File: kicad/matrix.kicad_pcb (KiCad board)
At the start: 2 copper layers, 76.2 x 76.2 mm, 20 parts, among them J1 Conn_01x08, U1 TLC59025, U10 P-FET, U11 P-FET, U2 74HC595, U3 74HC595, U4 P-FET, U5 P-FET, U6 P-FET, U7 P-FET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

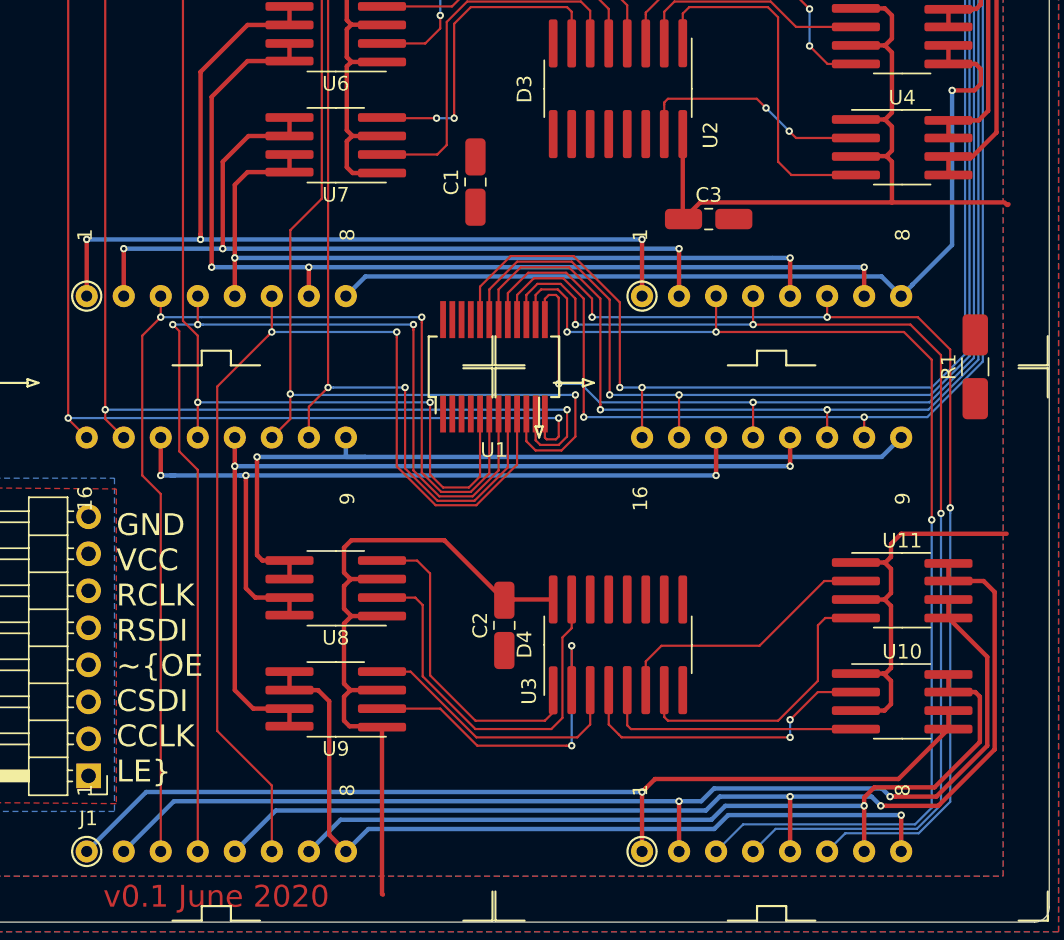
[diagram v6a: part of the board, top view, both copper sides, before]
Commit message: Wire up everything but ground net
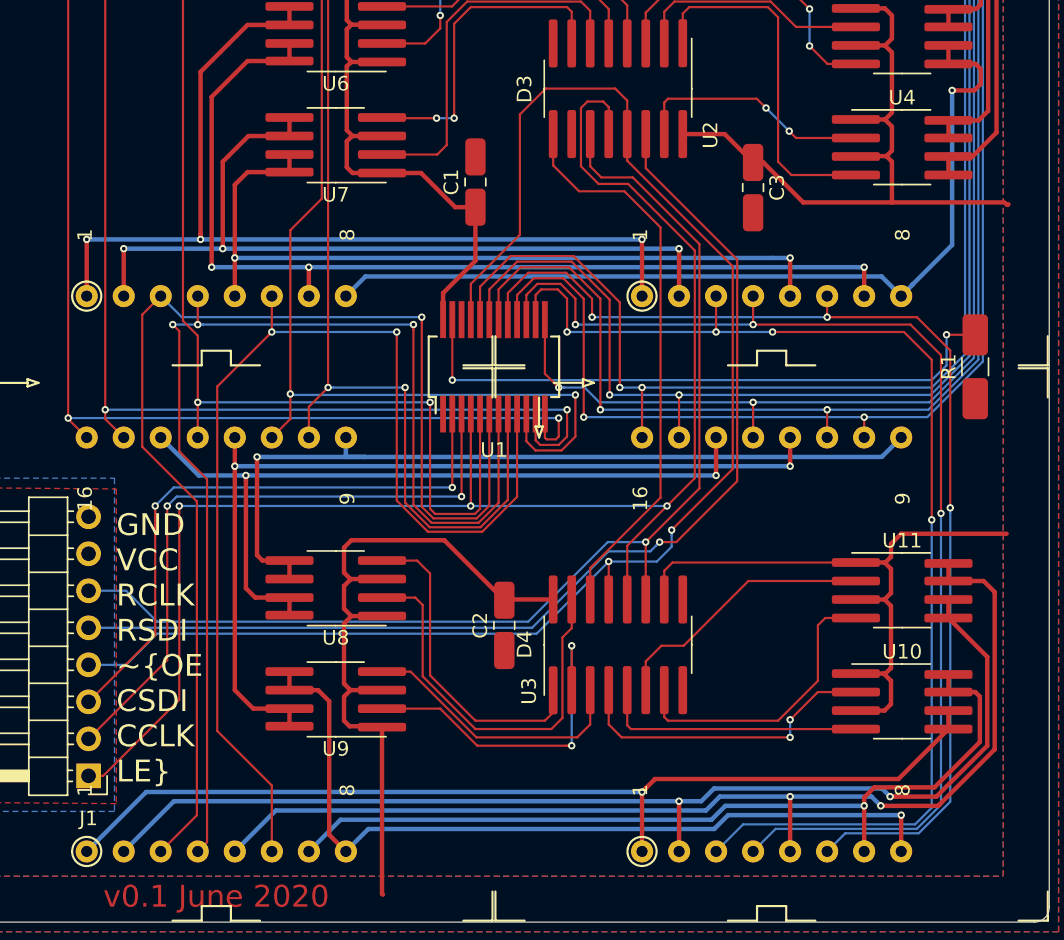
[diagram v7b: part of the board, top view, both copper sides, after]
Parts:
- moved C3 3.74 mm to (208.2, 63.1), turned to 270 degrees
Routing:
- net /~OE: track 0.00 -> 106.7 mm, vias 0 -> 2
- net /LE: track 0.00 -> 105.6 mm, vias 0 -> 3
- net /ROWCLK: track 0.00 -> 79.2 mm, vias 0 -> 1
- net /ROWSDI: track 0.00 -> 75.1 mm, vias 0 -> 1
- net /COLCLK: track 0.00 -> 44.3 mm, vias 0 -> 2
- net Net-(R1-Pad2): track 0.00 -> 42.5 mm, vias 0 -> 2
- net /COLSDI: track 0.00 -> 41.3 mm, vias 0 -> 2
- net Net-(U2-Pad9): track 0.00 -> 38.8 mm
- net VDD: track 161.7 -> 190.8 mm
- net /COL1: track 77.5 -> 84.3 mm, vias 2 -> 1
- net /COL2: track 76.5 -> 81.2 mm
- net /COL4: track 73.0 -> 77.2 mm
- net /COL3: track 62.6 -> 66.8 mm
- net /COL0: track 68.2 -> 72.4 mm
- net /COL8: track 85.6 -> 82.1 mm
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
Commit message: Wire up remaining traces
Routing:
- net GND: track 0.00 -> 166.3 mm, vias 0 -> 7
- net VDD: track 190.8 -> 205.3 mm, vias 0 -> 2
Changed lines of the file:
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@@
   (general
     (thickness 1.6)
-    (drawings 12)
-    (tracks 816)
+    (drawings 13)
+    (tracks 859)
     (zones 0)
     (modules 20)
@@
   (page A4)
   (layers
-    (0 F.Cu signal)
-    (31 B.Cu signal)
-    (36 B.SilkS user hide)
-    (37 F.SilkS user hide)
+    (0 F.Cu signal hide)
+    (31 B.Cu signal hide)
+    (36 B.SilkS user)
+    (37 F.SilkS user)
     (38 B.Mask user)
     (39 F.Mask user)
@@
     (user_trace_width 0.1524)
     (user_trace_width 0.3048)
+    (user_trace_width 0.762)
     (trace_clearance 0.1524)
     (zone_clearance 0.508)
@@
     (descr "Through hole angled pin header, 1x08, 2.54mm pitch, 6mm pin length, single row")
     (tags "Through hole angled pin header THT 1x08 2.54mm single row")
-    (fp_text reference J1 (at 0 -2.921) (layer F.SilkS)
+    (fp_text reference J1 (at 0 20.1676) (layer F.SilkS)
       (effects (font (size 1 1) (thickness 0.15)))
     )
@@
   (module local:LED_8x8_3MM_38x38MM (layer F.Cu)
     (at 209.423 56.388 90)
-    (fp_text reference D3 (at 0 -16.95 90) (layer F.SilkS)
+    (fp_text reference D3 (at 14.3256 11.557 180) (layer F.SilkS)
       (effects (font (size 1 1) (thickness 0.15)))
     )
@@
   (module local:LED_8x8_3MM_38x38MM (layer F.Cu)
     (at 171.323 56.388 90)
-    (fp_text reference D1 (at 0 -16.95 90) (layer F.SilkS)
+    (fp_text reference D1 (at 14.1986 11.43 180) (layer F.SilkS)
       (effects (font (size 1 1) (thickness 0.15)))
     )
@@
   (module local:LED_8x8_3MM_38x38MM (layer F.Cu)
     (at 171.323 94.491 90)
-    (fp_text reference D2 (at 0 -16.95 90) (layer F.SilkS)
+    (fp_text reference D2 (at -14.2464 11.43 180) (layer F.SilkS)
       (effects (font (size 1 1) (thickness 0.15)))
     )
@@
   (module local:LED_8x8_3MM_38x38MM (layer F.Cu)
     (at 209.423 94.488 90)
-    (fp_text reference D4 (at 0 -16.95 90) (layer F.SilkS)
+    (fp_text reference D4 (at -14.2494 11.43 180) (layer F.SilkS)
       (effects (font (size 1 1) (thickness 0.15)))
     )
@@
     )
   )
+  (gr_text "v0.1 June 2020" (at 154.305 94.6404 270) (layer B.Cu)
+    (effects (font (size 1.5 1.5) (thickness 0.3)) (justify mirror))
+  )
   (gr_text "GND\nVCC\nRCLK\nRSDI\n~OE\nCSDI\nCCLK\nLE" (at 160.401 94.742) (layer B.SilkS)
     (effects (font (size 1.5 1.5) (thickness 0.3)) (justify left mirror))
@@
     (effects (font (size 1.5 1.5) (thickness 0.3)) (justify left))
   )
-  (gr_text "v0.1 June 2020" (at 171.323 111.7854) (layer F.Cu)
+  (gr_text "v0.1 June 2020" (at 156.972 74.7014 270) (layer F.Cu)
     (effects (font (size 1.5 1.5) (thickness 0.3)))
   )
@@
   (gr_line (start 227.457 113.538) (end 153.289 113.538) (layer Edge.Cuts) (width 0.05))
   (gr_line (start 228.473 38.354) (end 228.473 112.522) (layer Edge.Cuts) (width 0.05))
+  (via (at 189.103 55.9054) (size 0.508) (drill 0.254) (layers F.Cu B.Cu) (net 36))
+  (segment (start 154.813 55.9054) (end 189.103 55.9054) (width 0.762) (layer B.Cu) (net 36))
+  (segment (start 155.067 74.9554) (end 186.817 74.9554) (width 0.762) (layer B.Cu) (net 36))
+  (segment (start 186.817 74.9554) (end 186.817 75.7174) (width 0.762) (layer B.Cu) (net 36))
+  (via (at 205.867 97.5614) (size 0.508) (drill 0.254) (layers F.Cu B.Cu) (net 36))
+  (segment (start 163.957 105.4354) (end 166.751 102.6414) (width 0.762) (layer B.Cu) (net 36))
+  (segment (start 200.787 102.6414) (end 205.867 97.5614) (width 0.762) (layer B.Cu) (net 36))
   (segment (start 161.163 43.458) (end 162.433 42.188) (width 0.1524) (layer F.Cu) (net 1))
   (segment (start 161.163 79.021) (end 161.163 78.9559) (width 0.1524) (layer F.Cu) (net 1))
@@
   (segment (start 225.6282 64.3382) (end 225.679 64.2874) (width 0.3048) (layer F.Cu) (net 33))
   (segment (start 217.678 61.3664) (end 217.678 64.1604) (width 0.3048) (layer F.Cu) (net 33))
-  (segment (start 217.678 64.1604) (end 225.2218 64.1604) (width 0.3048) (layer F.Cu) (net 33))
   (segment (start 225.3996 64.1604) (end 225.5774 64.3382) (width 0.3048) (layer F.Cu) (net 33))
   (segment (start 191.6833 91.4019) (end 194.437 91.4019) (width 0.3048) (layer F.Cu) (net 33))
@@
   (segment (start 189.103 68.1609) (end 189.103 64.4884) (width 0.3048) (layer F.Cu) (net 33))
   (segment (start 186.8805 70.3834) (end 189.103 68.1609) (width 0.3048) (layer F.Cu) (net 33))
+  (segment (start 217.678 64.1604) (end 225.679 64.1604) (width 0.3048) (layer F.Cu) (net 33))
+  (via (at 191.389 63.5254) (size 0.508) (drill 0.254) (layers F.Cu B.Cu) (net 33))
+  (segment (start 190.426 64.4884) (end 191.389 63.5254) (width 0.3048) (layer F.Cu) (net 33))
+  (segment (start 189.103 64.4884) (end 190.426 64.4884) (width 0.3048) (layer F.Cu) (net 33))
+  (segment (start 193.167 61.7474) (end 193.167 59.2074) (width 0.3048) (layer B.Cu) (net 33))
+  (via (at 193.167 59.2074) (size 0.508) (drill 0.254) (layers F.Cu B.Cu) (net 33))
+  (segment (start 191.389 63.5254) (end 193.167 61.7474) (width 0.3048) (layer B.Cu) (net 33))
+  (segment (start 195.453 57.1754) (end 195.707 57.4294) (width 0.3048) (layer F.Cu) (net 33))
+  (segment (start 193.167 57.9374) (end 193.929 57.1754) (width 0.3048) (layer F.Cu) (net 33))
+  (segment (start 195.707 57.4294) (end 195.707 59.4726) (width 0.3048) (layer F.Cu) (net 33))
+  (segment (start 193.929 57.1754) (end 195.453 57.1754) (width 0.3048) (layer F.Cu) (net 33))
+  (segment (start 193.167 59.2074) (end 193.167 57.9374) (width 0.3048) (layer F.Cu) (net 33))
   (segment (start 198.247 91.4034) (end 198.247 89.9414) (width 0.1524) (layer F.Cu) (net 35))
   (segment (start 198.247 91.4034) (end 198.247 88.7984) (width 0.1524) (layer F.Cu) (net 35))
@@
   (segment (start 206.756 82.4484) (end 206.756 68.5419) (width 0.1524) (layer F.Cu) (net 35))
   (segment (start 202.565 86.6394) (end 206.756 82.4484) (width 0.1524) (layer F.Cu) (net 35))
+  (segment (start 203.389 97.5614) (end 203.327 97.6234) (width 0.3048) (layer F.Cu) (net 36))
+  (segment (start 205.867 97.5614) (end 203.389 97.5614) (width 0.3048) (layer F.Cu) (net 36))
+  (via (at 191.135 98.8314) (size 0.508) (drill 0.254) (layers F.Cu B.Cu) (net 36))
+  (segment (start 191.0842 98.7806) (end 191.135 98.8314) (width 0.3048) (layer F.Cu) (net 36))
+  (segment (start 191.0842 94.9049) (end 191.0842 98.7806) (width 0.3048) (layer F.Cu) (net 36))
+  (segment (start 191.135 102.6414) (end 200.787 102.6414) (width 0.762) (layer B.Cu) (net 36))
+  (segment (start 191.135 98.8314) (end 191.135 102.6414) (width 0.3048) (layer B.Cu) (net 36))
+  (segment (start 166.751 102.6414) (end 191.135 102.6414) (width 0.762) (layer B.Cu) (net 36))
+  (segment (start 186.8805 75.0189) (end 186.817 74.9554) (width 0.3048) (layer F.Cu) (net 36))
+  (via (at 186.817 74.9554) (size 0.508) (drill 0.254) (layers F.Cu B.Cu) (net 36))
+  (segment (start 186.8805 78.6765) (end 186.8805 75.0189) (width 0.3048) (layer F.Cu) (net 36))
+  (segment (start 186.817 75.7174) (end 186.817 75.7174) (width 0.762) (layer B.Cu) (net 36))
+  (via (at 186.817 75.7174) (size 0.508) (drill 0.254) (layers F.Cu B.Cu) (net 36))
+  (segment (start 189.103 61.0384) (end 189.103 55.9054) (width 0.762) (layer F.Cu) (net 36))
+  (segment (start 191.7842 55.9054) (end 194.437 53.2526) (width 0.3048) (layer F.Cu) (net 36))
+  (segment (start 189.103 55.9054) (end 191.7842 55.9054) (width 0.3048) (layer F.Cu) (net 36))
+  (via (at 205.359 64.2874) (size 0.508) (drill 0.254) (layers F.Cu B.Cu) (net 36))
+  (segment (start 205.359 64.2874) (end 205.867 64.7954) (width 0.3048) (layer F.Cu) (net 36))
+  (segment (start 205.867 64.7954) (end 208.079 64.7954) (width 0.3048) (layer F.Cu) (net 36))
+  (segment (start 208.079 64.7954) (end 208.153 64.8694) (width 0.3048) (layer F.Cu) (net 36))
+  (segment (start 196.977 55.9054) (end 205.359 64.2874) (width 0.762) (layer B.Cu) (net 36))
+  (segment (start 189.103 55.9054) (end 196.977 55.9054) (width 0.762) (layer B.Cu) (net 36))
+  (via (at 223.393 80.5434) (size 0.508) (drill 0.254) (layers F.Cu B.Cu) (net 36))
+  (segment (start 223.393 77.6255) (end 223.393 80.5434) (width 0.762) (layer F.Cu) (net 36))
+  (segment (start 223.393 80.5434) (end 226.441 80.5434) (width 0.762) (layer B.Cu) (net 36))
   (segment (start 194.437 61.6204) (end 194.437 59.4726) (width 0.1524) (layer F.Cu) (net 37))
   (segment (start 196.215 63.3984) (end 194.437 61.6204) (width 0.1524) (layer F.Cu) (net 37))
